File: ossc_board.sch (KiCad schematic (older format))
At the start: 4 parts

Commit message: update PCB
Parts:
- MH1, MH2, MH3, MH4: footprint Connect:1pin -> MountingHole:MountingHole_2.7mm_M2.5
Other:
- moved on the sheet: MH3
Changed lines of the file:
@@
 $Descr A4 11693 8268
 encoding utf-8
-Sheet 1 4
+Sheet 1 5
 Title "Open Source Scan Converter"
 Date "2017-07-03"
@@
 $EndDescr
 $Sheet
-S 4650 950  2100 4200
+S 4650 950  2100 6700
 U 54FE3A8C
 F0 "fpga1" 50
@@
 F62 "CLK27" I L 4650 4400 60
 F63 "RESET_N" O R 6750 4300 60
+F64 "MonCLKin" I L 4650 6150 60
+F65 "ToMon" I L 4650 6250 60
+F66 "FromMon" O L 4650 6350 60
+F67 "MC_SS" I L 4650 6600 60
+F68 "MC_MOSI" I L 4650 6700 60
+F69 "MC_MISO" O L 4650 6800 60
+F70 "MC_SCK" I L 4650 6900 60
+F71 "AudioOut_MCLK" I L 4650 7000 60
+F72 "AudioOut_BCK" O L 4650 7100 60
+F73 "AudioOut_LRCK" O L 4650 7200 60
+F74 "AudioOut_Data" O L 4650 7300 60
+F75 "Mic_BCLK" I R 6750 6150 60
+F76 "Mic_LRCK" I R 6750 6250 60
+F77 "Mic_Data" I R 6750 6350 60
+F78 "SPDIF_OUT" O R 6750 6450 60
 $EndSheet
 Text Notes 8900 5550 0    60   ~ 0
@@
 F35 "CLK27" O R 3050 4400 60
 F36 "5V" O R 3050 5900 60
+F37 "RGB3_VS" I L 1700 4300 60
+F38 "RGB3_HS" I L 1700 4200 60
+F39 "RGB3_G" I L 1700 3800 60
+F40 "RGB3_R" I L 1700 3700 60
+F41 "RGB3_B" I L 1700 3900 60
+F42 "5VDC_IN" I R 3050 6050 60
 $EndSheet
 Text Notes 5050 4850 0    60   ~ 0
@@
 F 0 "MH1" H 1330 950 40  0000 L CNN
 F 1 "CONN_1" H 1250 1005 30  0001 C CNN
-F 2 "Connect:1pin" H 1250 950 60  0001 C CNN
+F 2 "MountingHole:MountingHole_2.7mm_M2.5" H 1250 950 60  0001 C CNN
 F 3 "" H 1250 950 60  0000 C CNN
 	1    1250 950
@@
 L ossc_board-rescue:CONN_01X01 MH3
 U 1 1 55129B56
-P 1350 6250
-F 0 "MH3" H 1430 6250 40  0000 L CNN
-F 1 "CONN_1" H 1350 6305 30  0001 C CNN
-F 2 "Connect:1pin" H 1350 6250 60  0001 C CNN
-F 3 "" H 1350 6250 60  0000 C CNN
-	1    1350 6250
+P 1050 950
+F 0 "MH3" H 1130 950 40  0000 L CNN
+F 1 "CONN_1" H 1050 1005 30  0001 C CNN
+F 2 "MountingHole:MountingHole_2.7mm_M2.5" H 1050 950 60  0001 C CNN
+F 3 "" H 1050 950 60  0000 C CNN
+	1    1050 950
 	0    -1   -1   0
 $EndComp
@@
 F 0 "MH2" H 10530 1000 40  0000 L CNN
 F 1 "CONN_1" H 10450 1055 30  0001 C CNN
-F 2 "Connect:1pin" H 10450 1000 60  0001 C CNN
+F 2 "MountingHole:MountingHole_2.7mm_M2.5" H 10450 1000 60  0001 C CNN
 F 3 "" H 10450 1000 60  0000 C CNN
 	1    10450 1000
@@
 F 0 "MH4" H 10480 6200 40  0000 L CNN
 F 1 "CONN_1" H 10400 6255 30  0001 C CNN
-F 2 "Connect:1pin" H 10400 6200 60  0001 C CNN
+F 2 "MountingHole:MountingHole_2.7mm_M2.5" H 10400 6200 60  0001 C CNN
 F 3 "" H 10400 6200 60  0000 C CNN
 	1    10400 6200
@@
 Wire Wire Line
 	3050 5900 8350 5900
-NoConn ~ 1350 6450
+NoConn ~ 1050 1150
 NoConn ~ 1250 1150
 NoConn ~ 10450 1200
@@
 Wire Wire Line
 	3800 5550 8350 5550
+Wire Wire Line
+	1700 4200 1500 4200
+Wire Wire Line
+	1500 4200 1500 8400
+Wire Wire Line
+	1500 8400 1700 8400
+Wire Wire Line
+	1700 8500 1400 8500
+Wire Wire Line
+	1400 8500 1400 4300
+Wire Wire Line
+	1400 4300 1700 4300
+Wire Wire Line
+	1700 3700 1300 3700
+Wire Wire Line
+	1300 3700 1300 8700
+Wire Wire Line
+	1300 8700 1700 8700
+Wire Wire Line
+	1700 8800 1200 8800
+Wire Wire Line
+	1200 8800 1200 3800
+Wire Wire Line
+	1200 3800 1700 3800
+Wire Wire Line
+	1700 3900 1100 3900
+Wire Wire Line
+	1100 3900 1100 8900
+Wire Wire Line
+	1100 8900 1700 8900
+$Sheet
+S 1700 8000 1350 2750
+U 5F595115
+F0 "soundbox" 60
+F1 "soundbox.sch" 60
+F2 "HS_OUT" O L 1700 8400 60
+F3 "VS_OUT" O L 1700 8500 60
+F4 "RED_OUT" O L 1700 8700 60
+F5 "GREEN_OUT" O L 1700 8800 60
+F6 "BLUE_OUT" O L 1700 8900 60
+F7 "5VDC_OUT" O R 3050 8400 60
+$EndSheet
+Wire Wire Line
+	3050 6050 3350 6050
+Wire Wire Line
+	3350 6050 3350 8400
+Wire Wire Line
+	3350 8400 3050 8400
 $EndSCHEMATC

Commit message: update3
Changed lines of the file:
@@
 	8950 5700 9550 5700
-Wire Wire Line
-	3050 5550 3800 5550
 Wire Wire Line
 	3050 5650 8350 5650
@@
 Wire Notes Line
 	5950 4850 5950 4750
-Wire Wire Line
-	3800 4950 4650 4950
 Wire Wire Line
 	3050 4400 4650 4400
@@
 Connection ~ 6950 4300
 Wire Wire Line
-	3800 4950 3800 5550
-Connection ~ 3800 5550
-Wire Wire Line
 	3050 5900 8350 5900
 NoConn ~ 1050 1150
@@
 Wire Wire Line
 	6950 4300 8350 4300
-Wire Wire Line
-	3800 5550 8350 5550
 Wire Wire Line
 	1700 4200 1500 4200
@@
 F6 "BLUE_OUT" O L 1700 8900 60
 F7 "5VDC_OUT" O R 3050 8400 60
+F8 "VCCIO" I R 3050 8500 60
+F9 "SPDIF" I R 3050 8700 60
 $EndSheet
 Wire Wire Line
@@
 Wire Wire Line
 	3350 8400 3050 8400
+Wire Wire Line
+	6750 6450 7100 6450
+Wire Wire Line
+	7100 6450 7100 8700
+Wire Wire Line
+	7100 8700 3050 8700
+Wire Wire Line
+	3800 4950 4650 4950
+Wire Wire Line
+	3800 5550 8350 5550
+Connection ~ 3800 5550
+Wire Wire Line
+	3800 4950 3800 5550
+Wire Wire Line
+	3050 5550 3450 5550
+Wire Wire Line
+	3450 8500 3450 5550
+Wire Wire Line
+	3450 8500 3050 8500
+Connection ~ 3450 5550
+Wire Wire Line
+	3450 5550 3800 5550
 $EndSCHEMATC

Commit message: add dxf update pcb
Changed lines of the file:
@@
 F65 "ToMon" I L 4650 6250 60
 F66 "FromMon" O L 4650 6350 60
-F67 "MC_SS" I L 4650 6600 60
-F68 "MC_MOSI" I L 4650 6700 60
-F69 "MC_MISO" O L 4650 6800 60
-F70 "MC_SCK" I L 4650 6900 60
+F67 "MC_SS" I R 6750 7050 60
+F68 "MC_MOSI" I R 6750 7150 60
+F69 "MC_MISO" O R 6750 7250 60
+F70 "MC_SCK" I R 6750 7350 60
 F71 "AudioOut_MCLK" I L 4650 7000 60
 F72 "AudioOut_BCK" O L 4650 7100 60
@@
 	3050 4300 4150 4300
 Wire Wire Line
-	3050 4600 4350 4600
-Wire Wire Line
-	3050 4700 4500 4700
+	3050 4700 3600 4700
 Wire Wire Line
 	6750 1050 8350 1050
@@
 F8 "VCCIO" I R 3050 8500 60
 F9 "SPDIF" I R 3050 8700 60
+F10 "SCL" I R 3050 8900 60
+F11 "SDA" B R 3050 9000 60
+F12 "Audio_MCK" O R 3050 9200 60
+F13 "Audio_BCK" I R 3050 9300 60
+F14 "Audio_LRCK" I R 3050 9400 60
+F15 "Audio_DATA" I R 3050 9500 60
+F16 "Mon_CLK" O R 3050 10400 60
+F17 "To_Mon" O R 3050 10500 60
+F18 "From_Mon" I R 3050 10600 60
+F19 "To_KBD" I R 3050 10300 60
+F20 "From_KBD" O R 3050 10200 60
 $EndSheet
 Wire Wire Line
@@
 Wire Wire Line
 	3450 5550 3800 5550
+Wire Wire Line
+	3050 4600 3700 4600
+Wire Wire Line
+	3050 8900 3600 8900
+Wire Wire Line
+	3600 8900 3600 4700
+Connection ~ 3600 4700
+Wire Wire Line
+	3600 4700 4500 4700
+Wire Wire Line
+	3700 4600 3700 9000
+Wire Wire Line
+	3700 9000 3050 9000
+Connection ~ 3700 4600
+Wire Wire Line
+	3700 4600 4350 4600
+Wire Wire Line
+	4650 6150 3900 6150
+Wire Wire Line
+	3900 6150 3900 10400
+Wire Wire Line
+	3900 10400 3050 10400
+Wire Wire Line
+	4650 6250 4000 6250
+Wire Wire Line
+	4000 6250 4000 10500
+Wire Wire Line
+	4000 10500 3050 10500
+Wire Wire Line
+	3050 10600 4100 10600
+Wire Wire Line
+	4100 10600 4100 6350
+Wire Wire Line
+	4100 6350 4650 6350
+Wire Wire Line
+	3050 9200 4200 9200
+Wire Wire Line
+	4200 9200 4200 7000
+Wire Wire Line
+	4200 7000 4650 7000
+Wire Wire Line
+	4650 7100 4300 7100
+Wire Wire Line
+	4300 7100 4300 9300
+Wire Wire Line
+	4300 9300 3050 9300
+Wire Wire Line
+	4650 7200 4400 7200
+Wire Wire Line
+	4400 7200 4400 9400
+Wire Wire Line
+	4400 9400 3050 9400
+Wire Wire Line
+	3050 9500 4500 9500
+Wire Wire Line
+	4500 9500 4500 7300
+Wire Wire Line
+	4500 7300 4650 7300
 $EndSCHEMATC

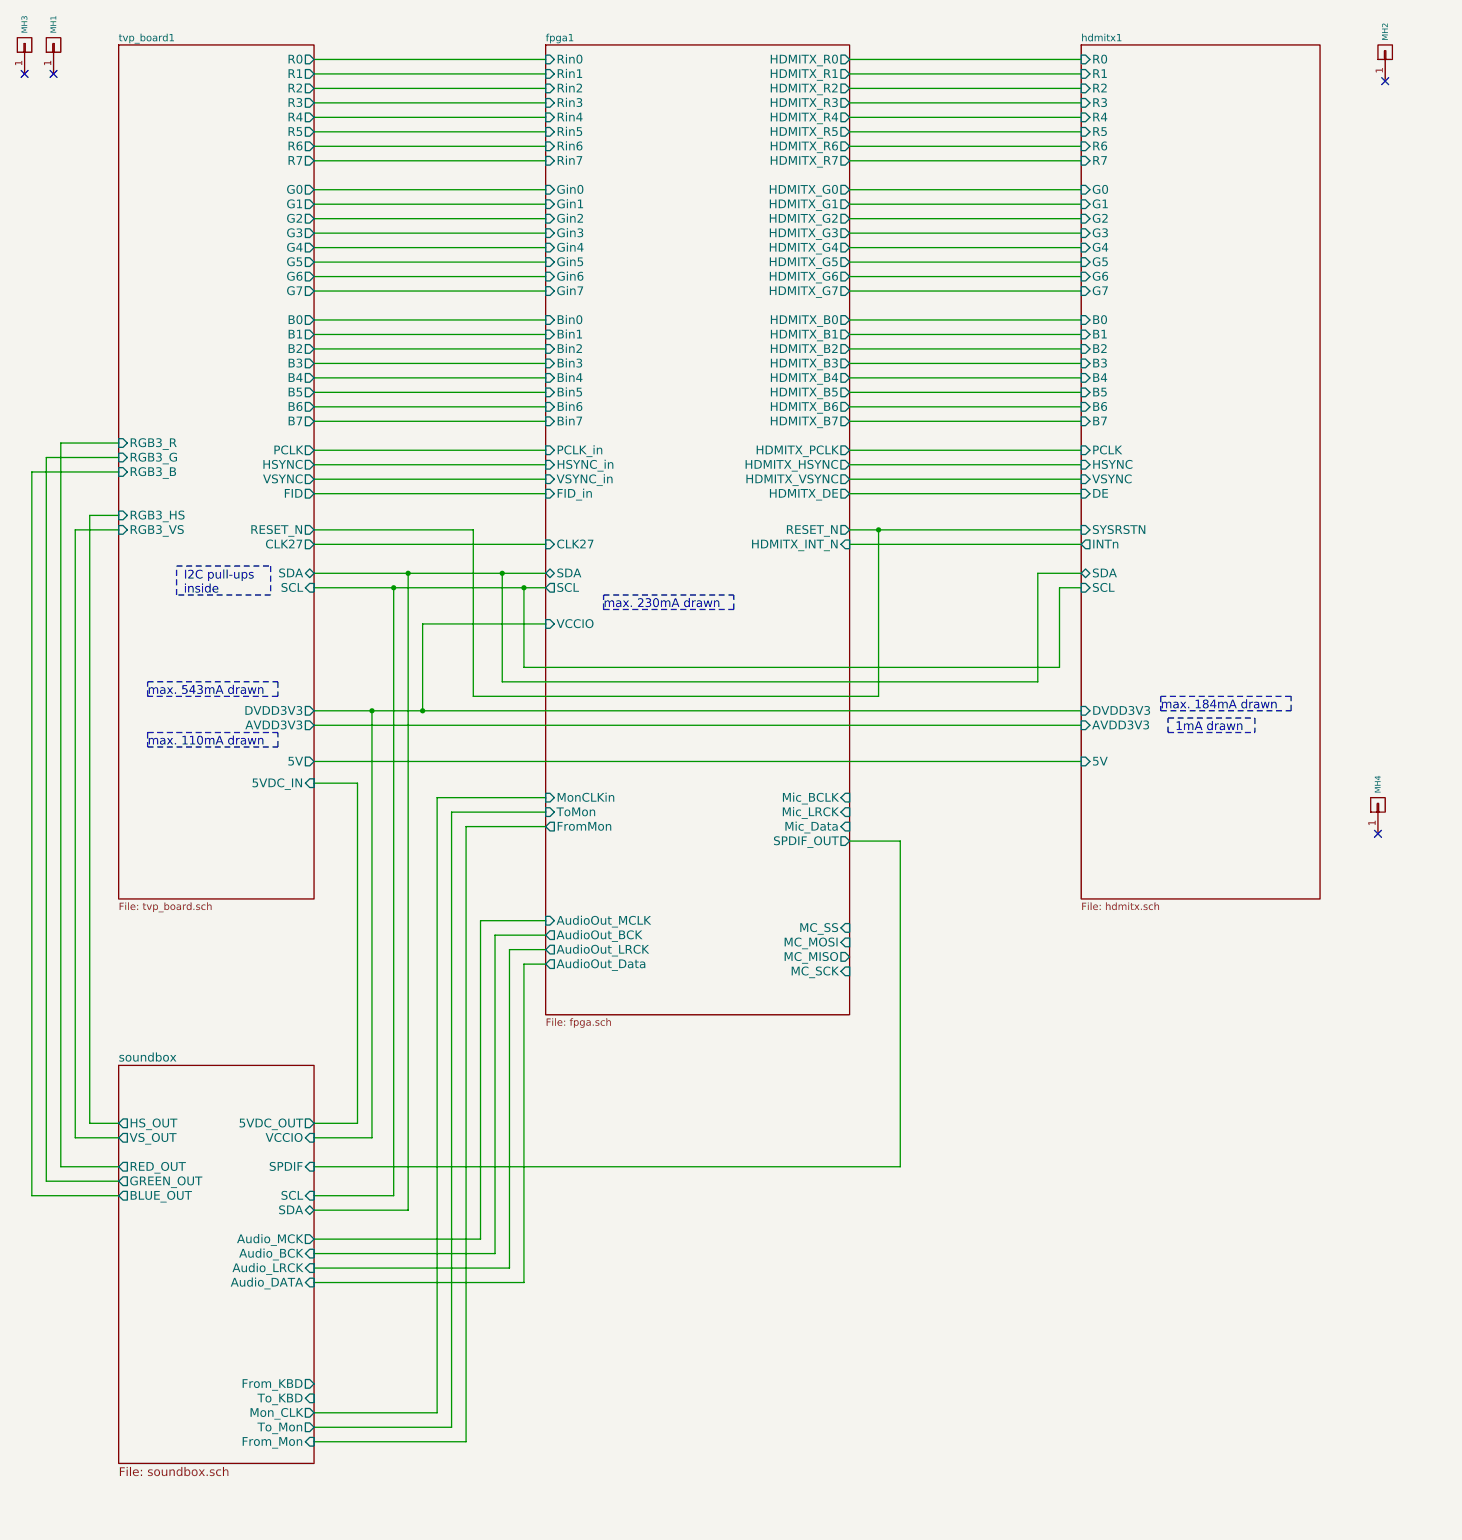
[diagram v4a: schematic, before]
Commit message: add adc
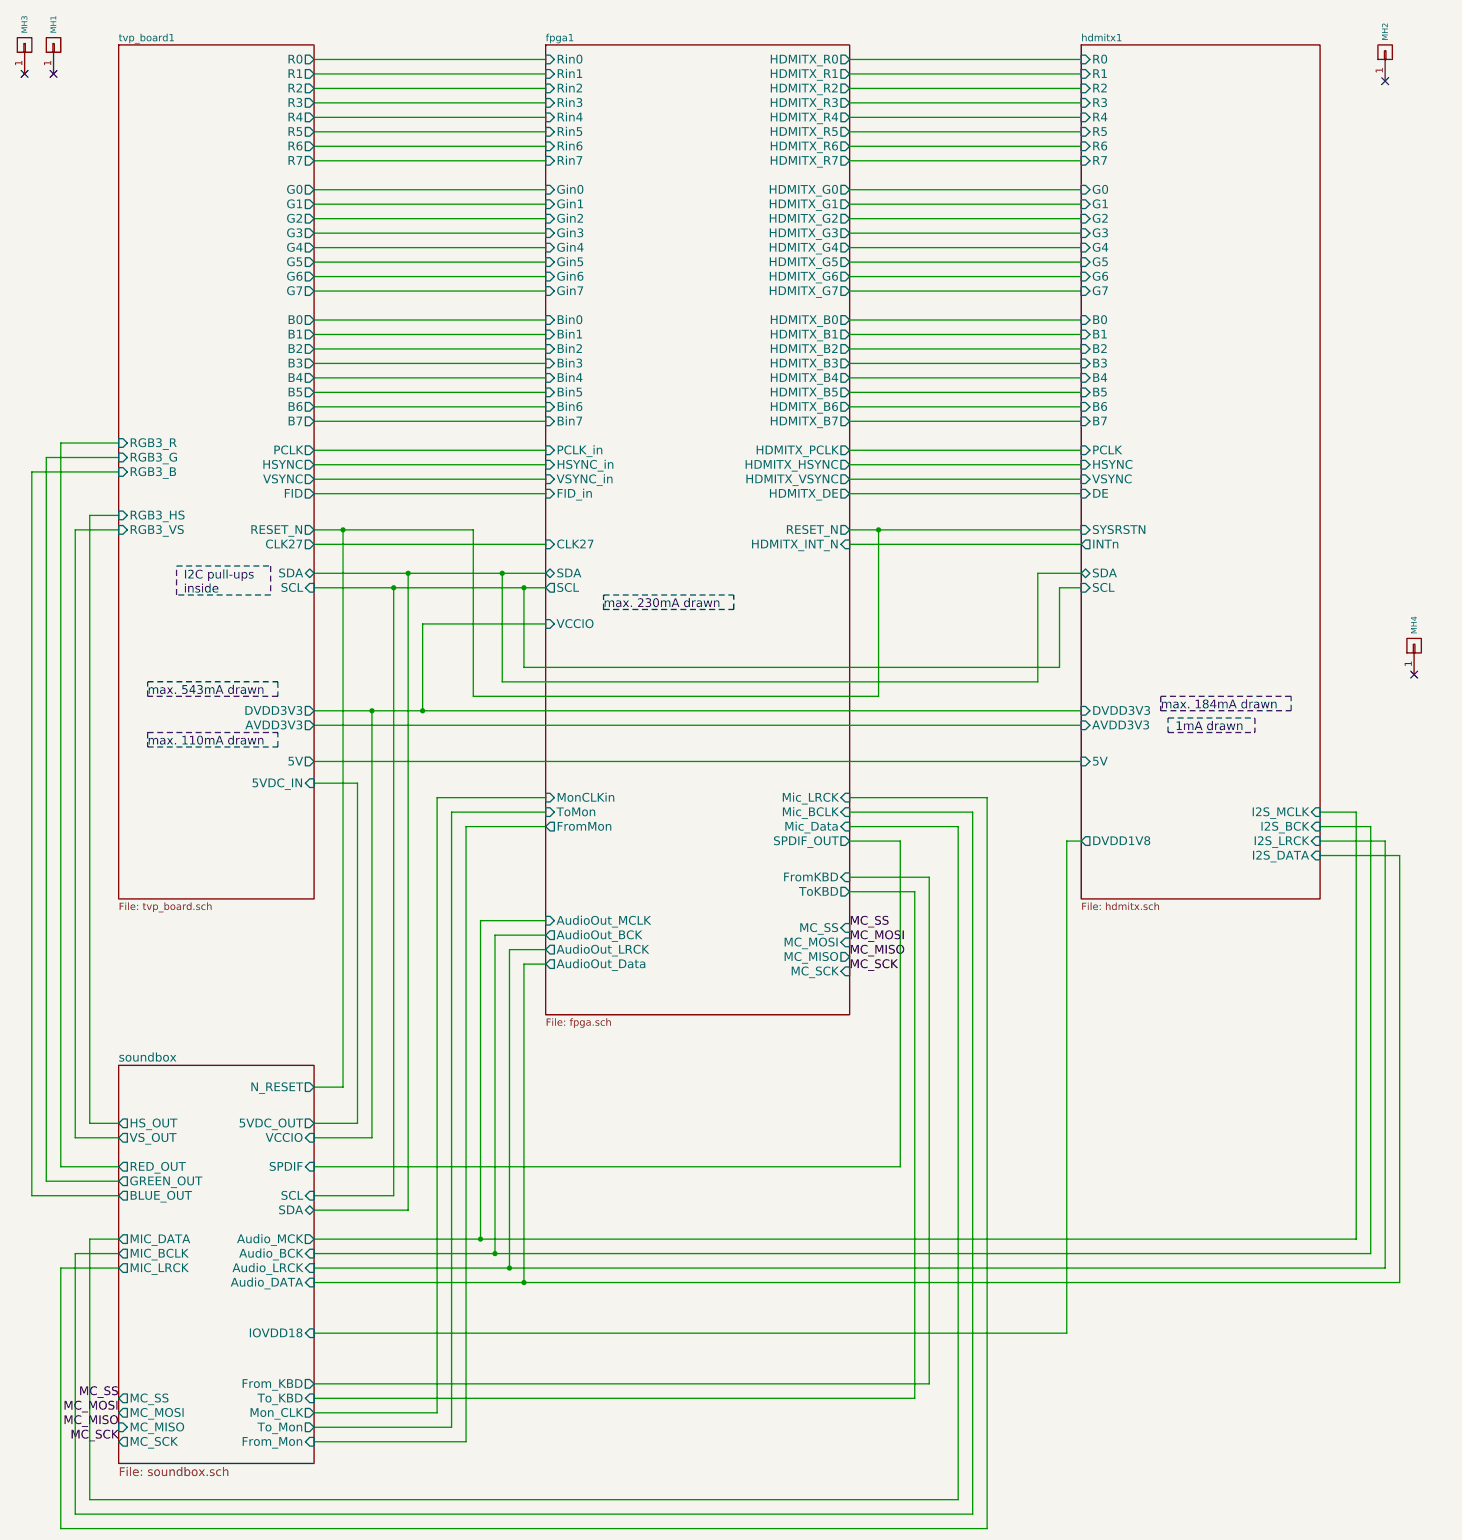
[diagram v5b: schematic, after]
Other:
- moved on the sheet: MH4
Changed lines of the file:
@@
 F73 "AudioOut_LRCK" O L 4650 7200 60
 F74 "AudioOut_Data" O L 4650 7300 60
-F75 "Mic_BCLK" I R 6750 6150 60
-F76 "Mic_LRCK" I R 6750 6250 60
+F75 "Mic_BCLK" I R 6750 6250 60
+F76 "Mic_LRCK" I R 6750 6150 60
 F77 "Mic_Data" I R 6750 6350 60
 F78 "SPDIF_OUT" O R 6750 6450 60
+F79 "FromKBD" I R 6750 6700 60
+F80 "ToKBD" O R 6750 6800 60
 $EndSheet
 Text Notes 8900 5550 0    60   ~ 0
@@
 F35 "AVDD3V3" I L 8350 5650 60
 F36 "5V" I L 8350 5900 60
+F37 "DVDD1V8" O L 8350 6450 60
+F38 "I2S_MCLK" I R 10000 6250 60
+F39 "I2S_DATA" I R 10000 6550 60
+F40 "I2S_LRCK" I R 10000 6450 60
+F41 "I2S_BCK" I R 10000 6350 60
 $EndSheet
 $Comp
@@
 L ossc_board-rescue:CONN_01X01 MH4
 U 1 1 5512E422
-P 10400 6200
-F 0 "MH4" H 10480 6200 40  0000 L CNN
-F 1 "CONN_1" H 10400 6255 30  0001 C CNN
-F 2 "MountingHole:MountingHole_2.7mm_M2.5" H 10400 6200 60  0001 C CNN
-F 3 "" H 10400 6200 60  0000 C CNN
-	1    10400 6200
+P 10650 5100
+F 0 "MH4" H 10730 5100 40  0000 L CNN
+F 1 "CONN_1" H 10650 5155 30  0001 C CNN
+F 2 "MountingHole:MountingHole_2.7mm_M2.5" H 10650 5100 60  0001 C CNN
+F 3 "" H 10650 5100 60  0000 C CNN
+	1    10650 5100
 	0    -1   -1   0
 $EndComp
@@
 	3050 4050 4650 4050
 Wire Wire Line
-	3050 4300 4150 4300
+	3050 4300 3250 4300
 Wire Wire Line
 	3050 4700 3600 4700
@@
 NoConn ~ 1250 1150
 NoConn ~ 10450 1200
-NoConn ~ 10400 6400
+NoConn ~ 10650 5300
 Wire Wire Line
 	4500 4700 4650 4700
@@
 F19 "To_KBD" I R 3050 10300 60
 F20 "From_KBD" O R 3050 10200 60
+F21 "N_RESET" O R 3050 8150 60
+F22 "IOVDD18" I R 3050 9850 60
+F23 "MIC_DATA" O L 1700 9200 60
+F24 "MIC_BCLK" O L 1700 9300 60
+F25 "MIC_LRCK" O L 1700 9400 60
+F26 "MC_SCK" O L 1700 10600 60
+F27 "MC_MISO" I L 1700 10500 60
+F28 "MC_MOSI" O L 1700 10400 60
+F29 "MC_SS" O L 1700 10300 60
 $EndSheet
 Wire Wire Line
@@
 Wire Wire Line
 	4500 7300 4650 7300
+Wire Wire Line
+	6750 6800 7200 6800
+Wire Wire Line
+	7200 6800 7200 10300
+Wire Wire Line
+	7200 10300 3050 10300
+Wire Wire Line
+	3050 10200 7300 10200
+Wire Wire Line
+	7300 10200 7300 6700
+Wire Wire Line
+	7300 6700 6750 6700
+Wire Wire Line
+	3050 8150 3250 8150
+Wire Wire Line
+	3250 8150 3250 4300
+Connection ~ 3250 4300
+Wire Wire Line
+	3250 4300 4150 4300
+Wire Wire Line
+	8350 6450 8250 6450
+Wire Wire Line
+	8250 6450 8250 9850
+Wire Wire Line
+	8250 9850 3050 9850
+Wire Wire Line
+	6750 6350 7500 6350
+Wire Wire Line
+	7500 6350 7500 11000
+Wire Wire Line
+	7500 11000 1500 11000
+Wire Wire Line
+	1500 11000 1500 9200
+Wire Wire Line
+	1500 9200 1700 9200
+Wire Wire Line
+	1700 9300 1400 9300
+Wire Wire Line
+	1400 9300 1400 11100
+Wire Wire Line
+	1400 11100 7600 11100
+Wire Wire Line
+	7600 11100 7600 6250
+Wire Wire Line
+	7700 11200 1300 11200
+Wire Wire Line
+	1300 11200 1300 9400
+Wire Wire Line
+	1300 9400 1700 9400
+Wire Wire Line
+	7600 6250 6750 6250
+Wire Wire Line
+	6750 6150 7700 6150
+Wire Wire Line
+	7700 6150 7700 11200
+Text Label 6750 7050 0    60   ~ 0
+MC_SS
+Text Label 1700 10300 2    60   ~ 0
+MC_SS
+Text Label 6750 7150 0    60   ~ 0
+MC_MOSI
+Text Label 1700 10400 2    60   ~ 0
+MC_MOSI
+Text Label 6750 7250 0    60   ~ 0
+MC_MISO
+Text Label 6750 7350 0    60   ~ 0
+MC_SCK
+Text Label 1700 10600 2    60   ~ 0
+MC_SCK
+Text Label 1700 10500 2    60   ~ 0
+MC_MISO
+Wire Wire Line
+	10000 6250 10250 6250
+Wire Wire Line
+	10250 6250 10250 9200
+Wire Wire Line
+	10250 9200 4200 9200
+Connection ~ 4200 9200
+Wire Wire Line
+	10350 9300 10350 6350
+Wire Wire Line
+	10350 6350 10000 6350
+Wire Wire Line
+	10000 6450 10450 6450
+Wire Wire Line
+	10450 6450 10450 9400
+Wire Wire Line
+	10450 9400 4400 9400
+Connection ~ 4400 9400
+Wire Wire Line
+	4300 9300 10350 9300
+Connection ~ 4300 9300
+Wire Wire Line
+	10000 6550 10550 6550
+Wire Wire Line
+	10550 6550 10550 9500
+Wire Wire Line
+	10550 9500 4500 9500
+Connection ~ 4500 9500
 $EndSCHEMATC

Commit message: update tracks
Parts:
- added MH5: CONN_1, MountingHole:MountingHole_2.7mm_M2.5, symbol ossc_board-rescue:CONN_01X01
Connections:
- no-connect marks 4 -> 5
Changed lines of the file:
@@
 	10550 9500 4500 9500
 Connection ~ 4500 9500
+$Comp
+L ossc_board-rescue:CONN_01X01 MH5
+U 1 1 5F49D208
+P 10850 5100
+F 0 "MH5" H 10930 5100 40  0000 L CNN
+F 1 "CONN_1" H 10850 5155 30  0001 C CNN
+F 2 "MountingHole:MountingHole_2.7mm_M2.5" H 10850 5100 60  0001 C CNN
+F 3 "" H 10850 5100 60  0000 C CNN
+	1    10850 5100
+	0    -1   -1   0
+$EndComp
+NoConn ~ 10850 5300
 $EndSCHEMATC
